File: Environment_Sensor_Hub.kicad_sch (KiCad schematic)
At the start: 0 parts

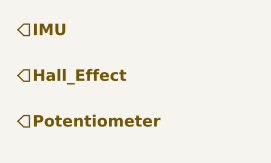
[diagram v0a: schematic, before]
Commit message: Updated Controls + Telemetry
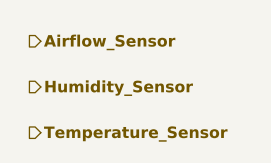
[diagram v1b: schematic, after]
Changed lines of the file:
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@@
 	(generator_version "9.0")
 	(paper "A4")
-	(hierarchical_label "IMU"
-		(shape input)
-		(at 138.43 95.25 0)
+	(hierarchical_label "Humidity_Sensor"
+		(shape output)
+		(at 139.7 101.6 0)
 		(effects
 			(font
@@
 		)
 	)
-	(hierarchical_label "Potentiometer"
-		(shape input)
-		(at 138.43 105.41 0)
+	(hierarchical_label "Temperature_Sensor"
+		(shape output)
+		(at 139.7 106.68 0)
 		(effects
 			(font
@@
 		)
 	)
-	(hierarchical_label "Hall_Effect"
-		(shape input)
-		(at 138.43 100.33 0)
+	(hierarchical_label "Airflow_Sensor"
+		(shape output)
+		(at 139.7 96.52 0)
 		(effects
 			(font
